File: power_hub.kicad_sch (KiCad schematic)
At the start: 21 parts, among them Q1 SM4185

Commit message: v2
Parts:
- removed Q1: SM4185, Package_TO_SOT_SMD:TO-252-2, symbol Simulation_SPICE:PMOS
- removed R3: 1K, Resistor_SMD:R_2010_5025Metric_Pad1.40x2.65mm_HandSolder, symbol Device:R
- removed xt60-male1: Conn_01x02_Pin, Connector_AMASS:AMASS_XT60-M_1x02_P7.20mm_Vertical, symbol Connector:Conn_01x02_Pin
- added D3: D, Diode_SMD:D_SMA, symbol Device:D
- added F1, F2, F3, F4: Polyfuse, Fuse:Fuse_Bourns_MF-SM_7.98x5.44mm, symbol Device:Polyfuse
- added LED1, LED2: GREEN, LED_SMD:LED_0805_2012Metric, symbol Device:LED
- added ON/OFF1: Conn_01x02_Pin, Connector_JST:JST_XH_B2B-XH-AM_1x02_P2.50mm_Vertical, symbol Connector:Conn_01x02_Pin
- added Q1, Q4, Q5: 2N7002, Package_TO_SOT_SMD:SOT-23, symbol Transistor_FET:2N7002
- added Q3, Q6: SM4185, Package_TO_SOT_SMD:TO-252-2, symbol Simulation_SPICE:PMOS
- added R11: 10k, Resistor_SMD:R_2010_5025Metric_Pad1.40x2.65mm_HandSolder, symbol Device:R
- added R7: 5.1k, Resistor_SMD:R_2010_5025Metric_Pad1.40x2.65mm_HandSolder, symbol Device:R
- added R8, R9: 100R, Resistor_SMD:R_2010_5025Metric_Pad1.40x2.65mm_HandSolder, symbol Device:R
- added xt60-female3: Conn_01x02_Pin, Connector_AMASS:AMASS_XT60-M_1x02_P7.20mm_Vertical, symbol Connector:Conn_01x02_Pin
- R2: value 100R -> 5.1k
- xt60-female1, xt60-female2: footprint Connector_AMASS:AMASS_XT60-F_1x02_P7.20mm_Vertical -> Connector_AMASS:AMASS_XT60-M_1x02_P7.20mm_Vertical
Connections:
- net GND: now also AU1.1 (Pin_1), R2.2, D3.2 (A), ON/OFF1.1 (Pin_1), Q1.2 (S), Q5.2 (S), R7.2, xt60-female3.1 (Pin_1); no longer AU1.2 (Pin_2)
- net at R2.1: now also LED2.1 (K); no longer R1.2
- net 24v renamed Vbat_1
- net Vbat_1: now also D3.1 (K), LED1.2 (A), Q3.1 (D); no longer D1.1 (K)
- net Vbat renamed Vbat_2
- net Vbat_2: now also D1.1 (K), LED2.2 (A), Q6.1 (D); no longer R1.1
- new net: AU1.2 (Pin_2), R9.2
- new net: LED1.1 (K), R7.1
- new net: Q1.3 (D), Q6.2 (G), R1.2
- new net: Q3.2 (G), Q4.3 (D), R11.2
- new net: Q4.2 (S), Q5.3 (D)
- new net: ON/OFF1.2 (Pin_2), R8.2
- new net 24V_1: F1.2, F2.2, Q3.3 (S), R11.1
- new net 24V_2: F3.2, F4.2, Q6.3 (S), R1.1
- new net AU: Q5.1 (G), R9.1
- new net ON/OFF: Q1.1 (G), Q4.1 (G), R8.1
- new net V_IN: F1.1, F2.1, F3.1, F4.1, xt60-female3.2 (Pin_2)
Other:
- note added: "INPUT"
- note added: "ON/OFF"
- note added: "indication"
- moved on the sheet: xt30-female1, xt30-female2, xt30-female3, xt30-female4

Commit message: fix issue
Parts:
- added D2, D4: BZT52C15S, Diode_SMD:D_SOD-323, symbol Device:D_Zener
- added R3, R4, R5: 10k, Resistor_SMD:R_0805_2012Metric_Pad1.20x1.40mm_HandSolder, symbol Device:R
- R1, R11, R2, R7, R8, R9: footprint Resistor_SMD:R_2010_5025Metric_Pad1.40x2.65mm_HandSolder -> Resistor_SMD:R_0805_2012Metric_Pad1.20x1.40mm_HandSolder
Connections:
- net 24V_1: now also D2.1 (K)
- net 24V_2: now also D4.1 (K)
- net AU: now also R3.1
- net GND: now also R3.2, R5.2
- net ON/OFF: now also R4.1, R5.1
- net Vbat_1: now also Q3.2 (D); no longer Q3.1 (D)
- net Vbat_2: now also Q6.2 (D); no longer Q6.1 (D)
- net at Q1.3 (D), R1.2: now also Q6.1 (G), D4.2 (A); no longer Q6.2 (G)
- net at Q4.3 (D), R11.2: now also Q3.1 (G), D2.2 (A); no longer Q3.2 (G)
- net at Q4.2 (S), Q5.3 (D): now also R4.2
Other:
- moved on the sheet: Q5, R11

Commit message: reprise v2
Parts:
- added D5: BZT52C15S, Diode_SMD:D_SOD-323, symbol Device:D_Zener
- added D6: D, Diode_SMD:D_SMA, symbol Device:D
- added F5, F6: Polyfuse, Fuse:Fuse_Bourns_MF-SM_7.98x5.44mm, symbol Device:Polyfuse
- added LED3: GREEN, LED_SMD:LED_0805_2012Metric, symbol Device:LED
- added Q8: SM4185, Package_TO_SOT_SMD:TO-252-2, symbol Simulation_SPICE:PMOS
- added R12: 10k, Resistor_SMD:R_0805_2012Metric_Pad1.20x1.40mm_HandSolder, symbol Device:R
- added R13: 5.1k, Resistor_SMD:R_0805_2012Metric_Pad1.20x1.40mm_HandSolder, symbol Device:R
- added xt30-motor5, xt30-motor6, xt30-motor7, xt30-motor8: Conn_01x02_Pin, Connector_AMASS:AMASS_XT30U-F_1x02_P5.0mm_Vertical, symbol Connector:Conn_01x02_Pin
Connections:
- net 24V_2: now also D5.1 (K), F5.2, F6.2, Q8.3 (S), R12.1; no longer D4.1 (K), F3.2, F4.2, Q6.3 (S), R1.1
- net GND: now also D6.2 (A), R13.2, xt30-motor5.1 (Pin_1), xt30-motor6.1 (Pin_1), xt30-motor7.1 (Pin_1), xt30-motor8.1 (Pin_1)
- net V_IN: now also F5.1, F6.1
- net Vbat_1: now also D6.1 (K), Q8.2 (D), xt30-motor5.2 (Pin_2), xt30-motor6.2 (Pin_2), xt30-motor7.2 (Pin_2), xt30-motor8.2 (Pin_2); no longer D3.1 (K), Q3.2 (D), xt30-motor1.2 (Pin_2), xt30-motor2.2 (Pin_2), xt30-motor3.2 (Pin_2), xt30-motor4.2 (Pin_2)
- net on/off/au: now reaches D2.2 (A), Q3.1 (G), Q4.3 (D), R11.2
- net on/off/au: now also D5.2 (A), Q8.1 (G), R12.2
- new net: LED3.1 (K), R13.1
- new net 24V_3: D4.1 (K), F3.2, F4.2, Q6.3 (S), R1.1
- new net V_moteurs: D3.1 (K), LED3.2 (A), Q3.2 (D), xt30-motor1.2 (Pin_2), xt30-motor2.2 (Pin_2), xt30-motor3.2 (Pin_2), xt30-motor4.2 (Pin_2)
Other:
- note added: "AU + ON/OFF - OUTPUT"
- moved on the sheet: D1, D4, F3, F4, LED1, LED2, Q1, Q6, R1, R2, R5, R7

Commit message: update schematic and footprint, still a diode to choose
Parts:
- removed D1, D6: D, Diode_SMD:D_SMA, symbol Device:D
- removed F3, F4, F5, F6: Polyfuse, Fuse:Fuse_Bourns_MF-SM_7.98x5.44mm, symbol Device:Polyfuse
- added F10, F7, F8, F9: SMD1812-150C-33V 1812_SERI, Fuse:Fuse_Bourns_MF-SM_7.98x5.44mm, symbol Device:Polyfuse
- F1, F2: value Polyfuse -> SMD1812-150C-33V 1812_SERI
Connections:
- net Vbat_1 is gone; now on net GND: LED1.2 (A), Q8.2 (D), xt30-motor5.2 (Pin_2), xt30-motor6.2 (Pin_2), xt30-motor7.2 (Pin_2), xt30-motor8.2 (Pin_2)
- net Vbat_2 is gone; now on net GND: LED2.2 (A), Q6.2 (D), xt30-female1.2 (Pin_2), xt30-female2.2 (Pin_2), xt30-female3.2 (Pin_2), xt30-female4.2 (Pin_2), xt60-female1.2 (Pin_2), xt60-female2.2 (Pin_2)
- net 24V_2: now also F7.2, F8.2
- net 24V_3: now also F10.2, F9.2
- net V_IN: now also F10.1, F7.1, F8.1, F9.1
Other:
- note added: "A trouver quoi mettre la"

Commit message: update all
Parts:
- removed F10, F7: SMD1812-150C-33V 1812_SERI, Fuse:Fuse_Bourns_MF-SM_7.98x5.44mm, symbol Device:Polyfuse
- removed H1: MountingHole_Pad, MountingHole:MountingHole_3.2mm_M3_DIN965_Pad, symbol Mechanical:MountingHole_Pad
- removed LED1, LED2, LED3: GREEN, LED_SMD:LED_0805_2012Metric, symbol Device:LED
- removed R13, R2, R7: 5.1k, Resistor_SMD:R_0805_2012Metric_Pad1.20x1.40mm_HandSolder, symbol Device:R
- removed xt30-female4, xt30-motor8: Conn_01x02_Pin, Connector_AMASS:AMASS_XT30U-F_1x02_P5.0mm_Vertical, symbol Connector:Conn_01x02_Pin
- removed xt60-female1, xt60-female2, xt60-female3: Conn_01x02_Pin, Connector_AMASS:AMASS_XT60-M_1x02_P7.20mm_Vertical, symbol Connector:Conn_01x02_Pin
- added D1, D6, D7: D, Diode_SMD:D_SMA, symbol Device:D
- added J1: Conn_01x02_Pin, Connector_AMASS:AMASS_XT60-M_1x02_P7.20mm_Vertical, symbol Connector:Conn_01x02_Pin
- added Q2, Q7, Q9: SM4185, Package_TO_SOT_SMD:TO-252-2, symbol Simulation_SPICE:PMOS
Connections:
- net 24V_1: now also Q2.3 (S), Q7.3 (S), Q9.3 (S)
- net GND: now also D1.2 (A), D6.2 (A), D7.2 (A), J1.1 (Pin_1); no longer Q6.2 (D), Q8.2 (D), xt30-female1.2 (Pin_2), xt30-female2.2 (Pin_2), xt30-female3.2 (Pin_2), xt30-motor5.2 (Pin_2), xt30-motor6.2 (Pin_2), xt30-motor7.2 (Pin_2)
- net V_IN: now also J1.2 (Pin_2)
- net on/off/au: now also Q2.1 (G), Q7.1 (G), Q9.1 (G)
- net V_moteurs renamed V_moteurs_1
- net V_moteurs_1: no longer xt30-motor2.2 (Pin_2), xt30-motor3.2 (Pin_2), xt30-motor4.2 (Pin_2)
- new net V_moteurs_2: D1.1 (K), Q2.2 (D), xt30-motor2.2 (Pin_2)
- new net V_moteurs_3: D6.1 (K), Q7.2 (D), xt30-motor3.2 (Pin_2)
- new net V_moteurs_4: D7.1 (K), Q9.2 (D), xt30-motor4.2 (Pin_2)
- new net Vbat_1: Q8.2 (D), xt30-motor5.2 (Pin_2), xt30-motor6.2 (Pin_2), xt30-motor7.2 (Pin_2)
- new net Vbat_2: Q6.2 (D), xt30-female1.2 (Pin_2), xt30-female2.2 (Pin_2), xt30-female3.2 (Pin_2)
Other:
- note removed: "OUT - 3.3V"
- note removed: "OUT - 5V"
- note removed: "indication"
- moved on the sheet: D3, D5, F8, F9, Q8, R12

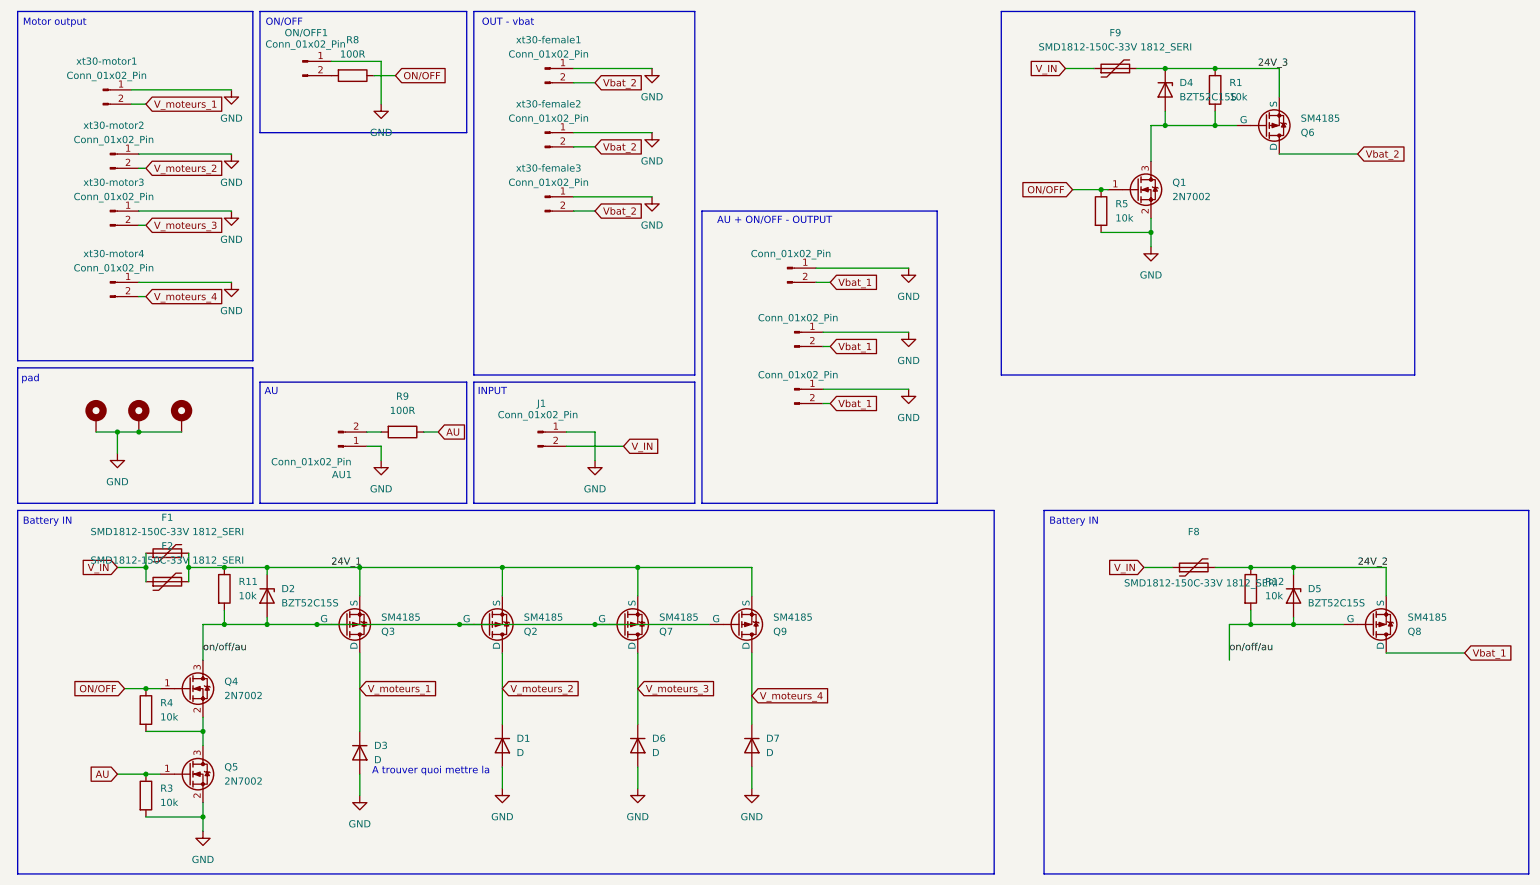
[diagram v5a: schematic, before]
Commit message: add serigraphy
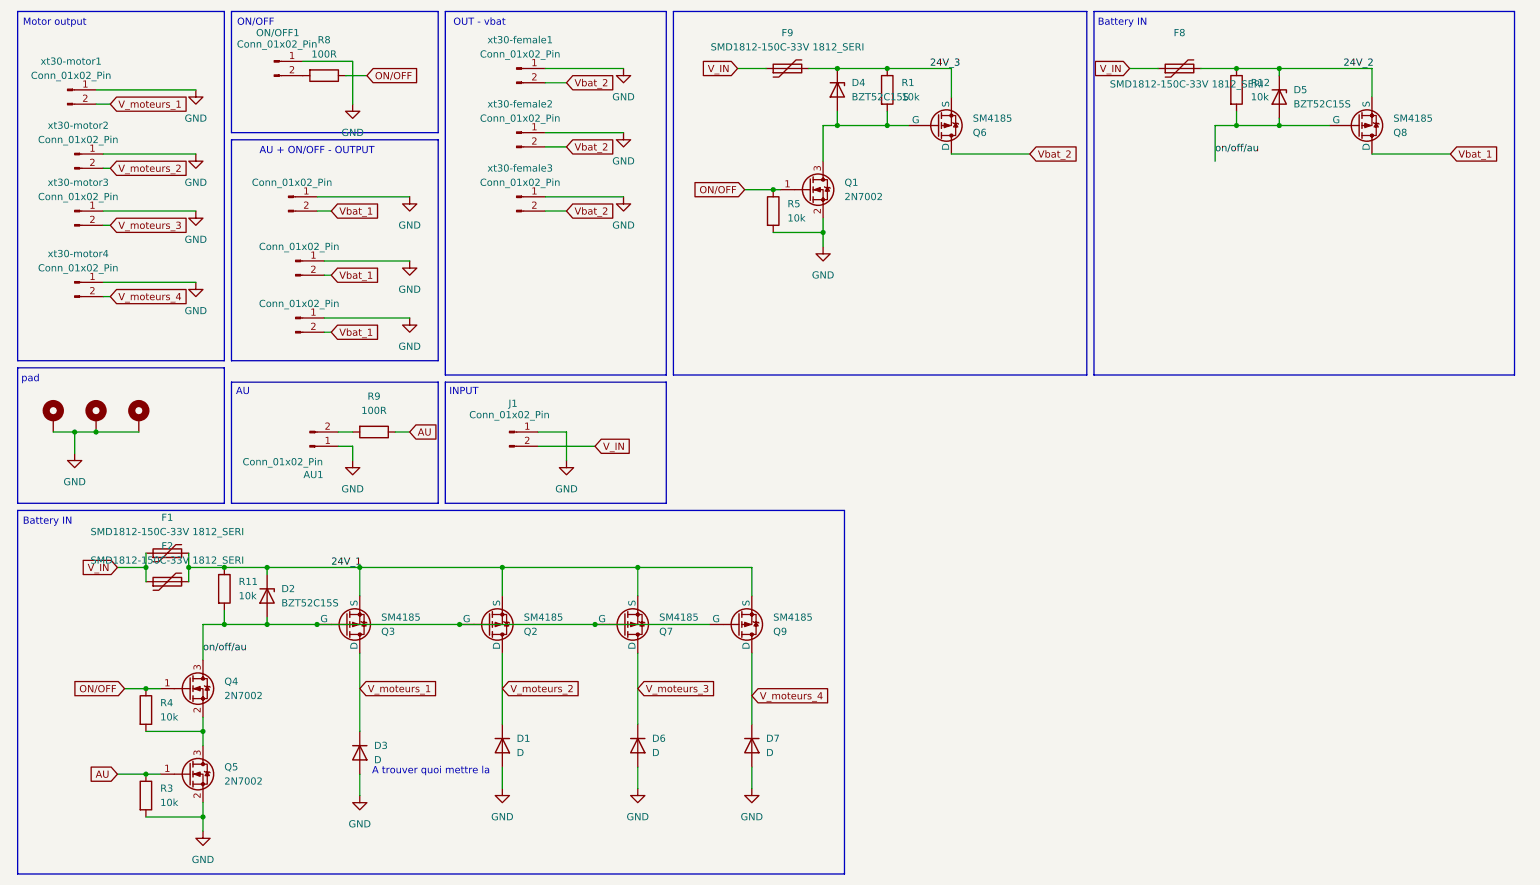
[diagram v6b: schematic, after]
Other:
- moved on the sheet: AU1, D4, D5, F8, F9, J1, ON/OFF1, Q1, Q6, Q8, R1, R12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
